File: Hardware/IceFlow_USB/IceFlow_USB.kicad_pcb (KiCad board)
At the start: 2 copper layers, 84 x 52.5 mm, 22 parts, among them J1 Barrel_Jack_Switch, J2 Conn_01x04, J3 TFT_Display_wTouch, J4 Conn_02x02_Odd_Even, J6 Conn_02x05_Odd_Even, J8 Power_Sw, U1 NCP1117-3.3_SOT223, U2 ESP32-WROVER-E

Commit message: Added second PCB with USB Power.
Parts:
- J1: value Barrel_Jack_Switch -> 10118194-0001LF; footprint Kitecraft_Barrel_Jacks:BarrelJack_Wuerth_6941xx301002 -> Kitecraft_Barrel_Jacks:USB_Micro_B_Female_10118194-0001LF
- moved J1 5.97 mm to (92.5, 125.9)
- moved J4 4.44 mm to (78.7, 123.4)
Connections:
- J1 pad 2: GND -> unconnected-(J1-Pad2)
- J1 pad 3: GND -> unconnected-(J1-Pad3)
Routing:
- net +3V3: track 105.7 -> 118.9 mm
- net Net-(J8-Pad1): track 0.00 -> 9.80 mm
- net /Vin: track 0.00 -> 9.63 mm
- net GND: track 28.9 -> 37.3 mm, vias 7 -> 9
- net /SSR_F: track 47.8 -> 44.5 mm
- net /SSR_O: track 45.7 -> 44.0 mm
- removed copper zone on F.Cu, net +3V3
- removed copper zone on F.Cu, net /Vin
- removed copper zone on F.Cu, net Net-(J8-Pad1)
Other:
- board text added: "V 1.1"
- board text removed: "V 1.0"

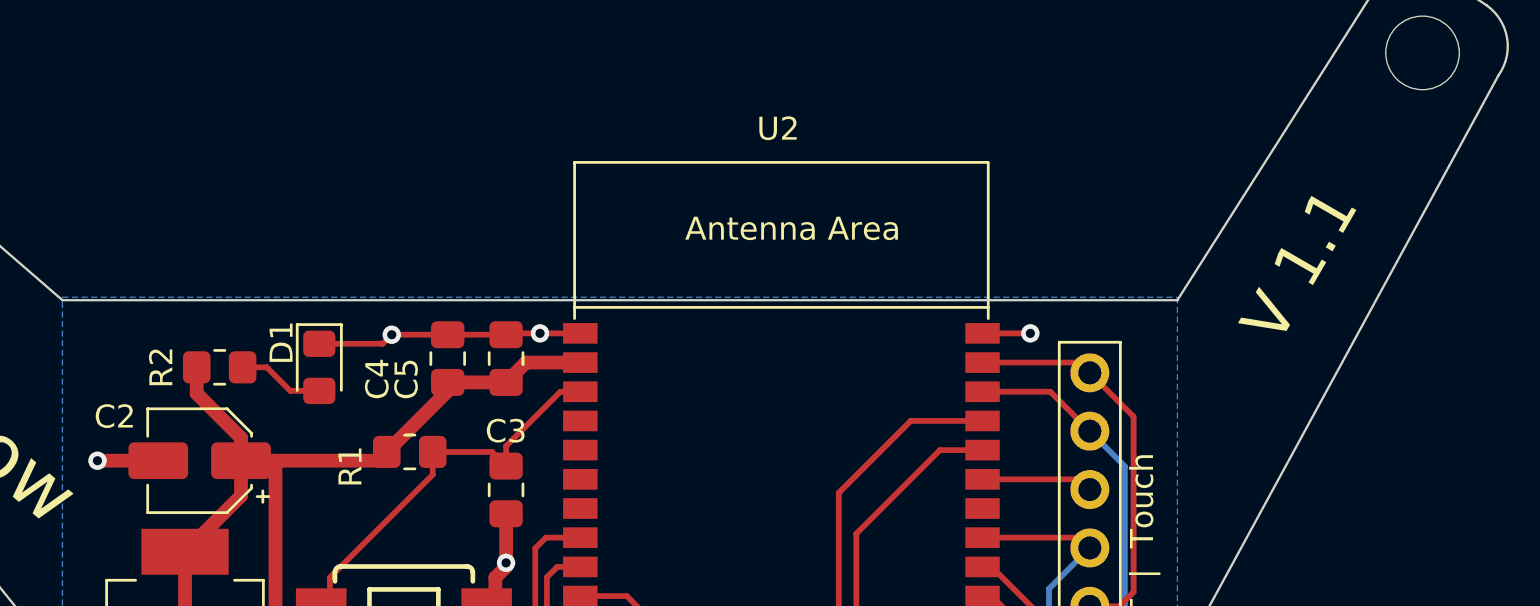
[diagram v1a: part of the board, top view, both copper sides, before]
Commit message: Pin map changes
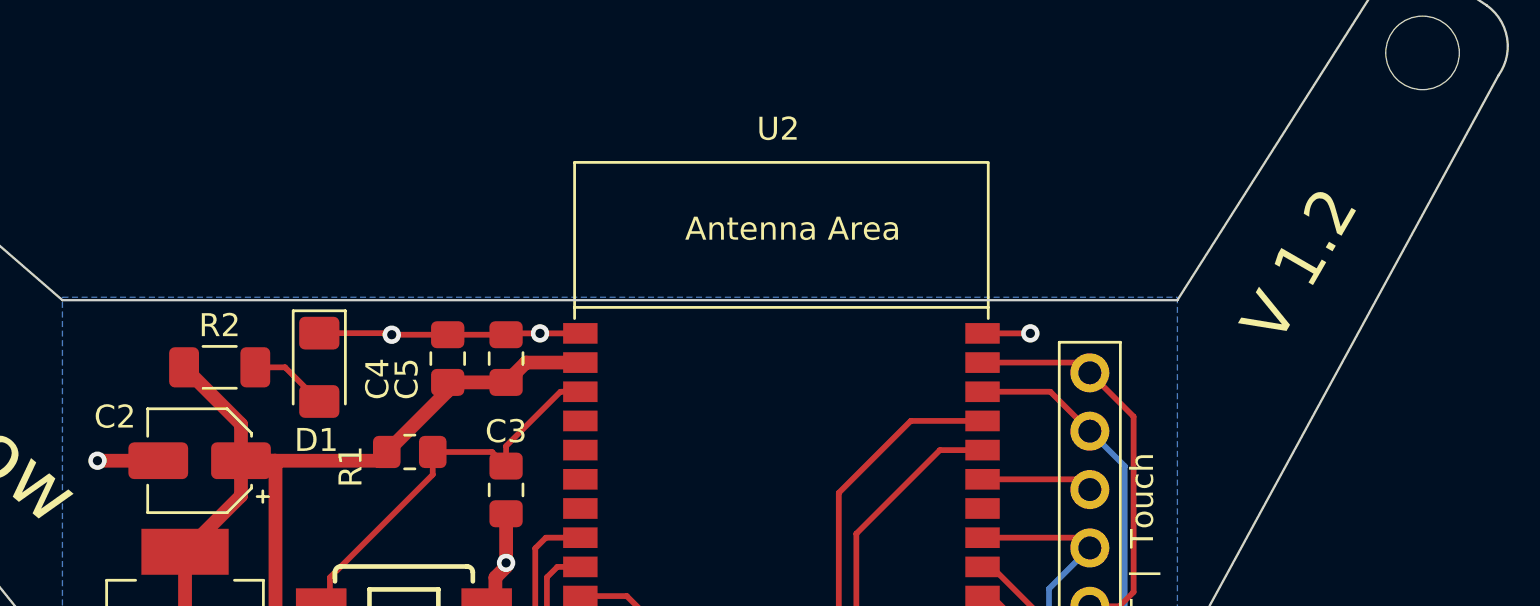
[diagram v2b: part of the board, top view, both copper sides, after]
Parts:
- D1: footprint LED_SMD:LED_0805_2012Metric_Pad1.15x1.40mm_HandSolder -> LED_SMD:LED_1206_3216Metric_Pad1.42x1.75mm_HandSolder
- R2: footprint Resistor_SMD:R_0805_2012Metric_Pad1.20x1.40mm_HandSolder -> Resistor_SMD:R_1206_3216Metric_Pad1.30x1.75mm_HandSolder
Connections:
- net /TFT_CS renamed /TOUCH_CS
- J6 pad 3: /TPB_CS -> /TPA_CS
- J6 pad 4: /TPA_CS -> /TPB_CS
- U2 pad 11: /TPB_CS -> /TPA_CS
- U2 pad 24: /TPA_CS -> /TPB_CS
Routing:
- net /TPB_CS: track 17.8 -> 28.1 mm, vias 0 -> 2
- net /TPA_CS: track 28.1 -> 17.8 mm, vias 2 -> 0
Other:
- board text added: "V 1.2"
- board text removed: "V 1.1"
